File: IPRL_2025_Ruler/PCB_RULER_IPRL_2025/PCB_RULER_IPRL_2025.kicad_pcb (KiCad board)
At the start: 2 copper layers, 155 x 30 mm, 23 parts, among them J102 USB_C_Receptacle_PowerOnly_6P, U101 NE555D, U102 4017

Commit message: Added NFC capabilities
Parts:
- added C102: 220n, Capacitor_SMD:C_0402_1005Metric, F.Cu at (90.5, 106.1)
- added C103: 470p, Capacitor_SMD:C_0402_1005Metric, F.Cu at (85.5, 107.9)
- added D111: LED_Small, LED_SMD:LED_0402_1005Metric, F.Cu at (91.0, 108.3)
- added IC1: NT3H2211W0FTTJ, ruler_footprints_2025:SOP65P490X110-8N, F.Cu at (88.0, 106.2)
- added R104: 47, Resistor_SMD:R_0402_1005Metric, F.Cu at (91.0, 104.0)
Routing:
- net Net-(IC1-LA): track 0.00 -> 10.8 mm, vias 0 -> 2
- net Net-(D111-K): track 0.00 -> 5.90 mm
- net Net-(IC1-VOUT): track 0.00 -> 5.81 mm
- net Net-(D111-A): track 0.00 -> 4.32 mm
- net /9: track 148.1 -> 145.2 mm
- net /1: track 0.00 -> 1.71 mm
- net /5: track 0.00 -> 1.70 mm
- net /TR: track 17.1 -> 18.0 mm
- net /4: track 140.2 -> 139.3 mm

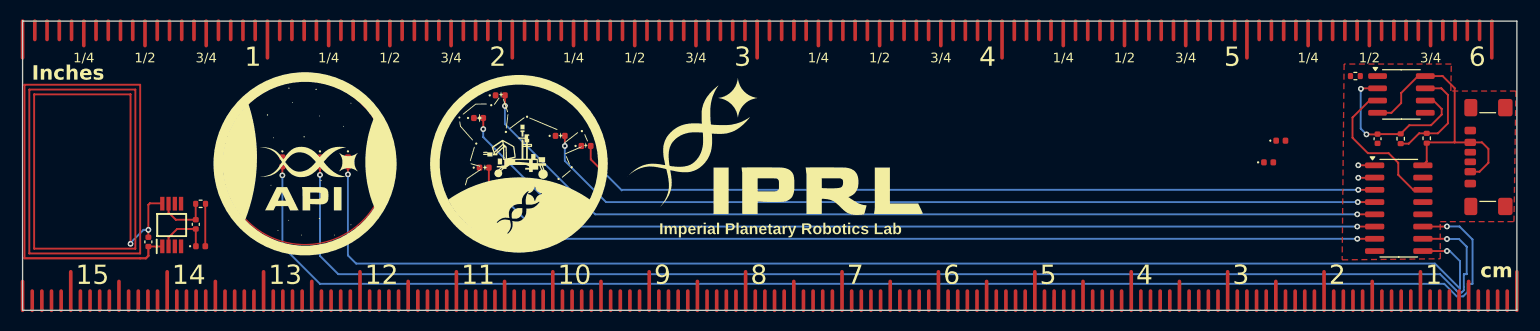
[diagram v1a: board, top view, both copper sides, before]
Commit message: Front side IPRL 2025 Ruler
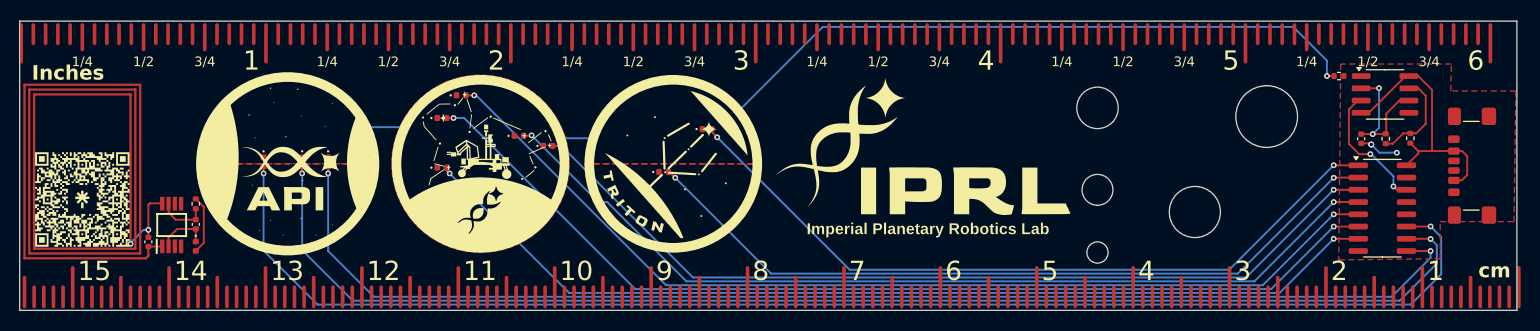
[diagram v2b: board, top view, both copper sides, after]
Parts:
- added G***: LOGO, ruler_footprints_2025:ICRS_LinktreeQR_10mm, F.Cu at (78.7, 103.5)
- added G***: LOGO, ruler_footprints_2025:Trition_Logo, F.Cu at (140.0, 99.8)
- added M2: MountingHole_2.2mm_M2, MountingHole:MountingHole_2.2mm_M2, F.Cu at (184.0, 109.0)
- added REF**: MountingHole_5.3mm_M5, MountingHole:MountingHole_5.3mm_M5, F.Cu at (194.1, 104.8)
- added REF**: MountingHole_4.3mm_M4, MountingHole:MountingHole_4.3mm_M4, F.Cu at (184.0, 94.0)
- added REF**: MountingHole_6.4mm_M6, MountingHole:MountingHole_6.4mm_M6, F.Cu at (201.6, 94.9)
- added REF**: MountingHole_3.2mm_M3, MountingHole:MountingHole_3.2mm_M3, F.Cu at (184.0, 102.5)
- moved D104 64.1 mm to (139.0, 100.6)
- moved D110 58.4 mm to (143.5, 96.2)
- moved G*** 15.3 mm to (166.0, 99.3)
- moved D106 4.39 mm to (116.0, 100.2)
- moved D103 4.26 mm to (124.0, 96.9)
- moved D105 4.05 mm to (118.0, 92.7)
- moved G*** 4.02 mm to (120.0, 99.9)
- moved D109 3.95 mm to (127.0, 98.0)
- moved D107 3.80 mm to (116.0, 95.0)
- moved G*** 3.77 mm to (120.0, 99.7)
- moved D108 2.05 mm to (104.2, 99.6)
- moved D102 1.95 mm to (97.5, 99.6)
- moved J102 1.92 mm to (224.0, 100.0)
- moved G*** 1.90 mm to (100.0, 99.8)
- moved D101 1.85 mm to (101.5, 99.6)
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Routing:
- net /1: track 1.71 -> 80.1 mm, vias 1 -> 2
- net /K: track 0.00 -> 76.7 mm, vias 0 -> 6
- net /5: track 1.70 -> 77.7 mm, vias 1 -> 2
- net /0: track 84.1 -> 93.0 mm
- net /2: track 88.4 -> 96.4 mm
- net /6: track 97.1 -> 103.8 mm
- net /3: track 95.9 -> 102.4 mm
- net /7: track 98.3 -> 104.6 mm
- net /4: track 139.3 -> 135.6 mm
- net /TR: track 18.0 -> 14.4 mm
- net GND: track 0.57 -> 4.10 mm, vias 0 -> 3
- net /8: track 133.1 -> 130.0 mm
- net /9: track 145.2 -> 142.4 mm
- net /CLK: track 15.7 -> 13.8 mm, vias 0 -> 2
- net Net-(D111-A): track 4.32 -> 6.08 mm
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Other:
- board size 155 x 30 mm -> 155.3 x 30 mm

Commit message: Added member names
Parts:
- removed the D104 at (139.0, 100.6)
- removed the D110 at (143.5, 96.2)
- removed the REF** at (201.6, 94.9)
- added D102: LED_Small, LED_SMD:LED_0402_1005Metric, F.Cu at (221.3, 108.8)
- added D106: LED_Small, LED_SMD:LED_0402_1005Metric, F.Cu at (138.9, 100.6)
- added D107: LED_Small, LED_SMD:LED_0402_1005Metric, F.Cu at (143.4, 96.2)
- added G***: LOGO, ruler_footprints_2025:STRAY_WIREFRAME, B.Cu at (169.7, 91.3)
- added G***: LOGO, ruler_footprints_2025:BOBCAT_WIREFRAME, B.Cu at (177.0, 90.3)
- added R103: 430, Resistor_SMD:R_0402_1005Metric, F.Cu at (221.3, 107.7)
- added REF**: PinHeader_1x04_P1.27mm_Vertical, Connector_PinHeader_1.27mm:PinHeader_1x04_P1.27mm_Vertical, F.Cu at (201.6, 109.1)
- added REF**: PinHeader_1x04_P2.00mm_Vertical, Connector_PinHeader_2.00mm:PinHeader_1x04_P2.00mm_Vertical, F.Cu at (205.0, 99.7)
- added REF**: MountingHole_2.7mm_M2.5_DIN965_Pad_TopBottom, MountingHole:MountingHole_2.7mm_M2.5_DIN965_Pad_TopBottom, F.Cu at (185.0, 100.5)
- added REF**: PinHeader_1x04_P2.54mm_Vertical, Connector_PinHeader_2.54mm:PinHeader_1x04_P2.54mm_Vertical, F.Cu at (201.6, 99.4)
- added REF**: PinHeader_1x04_P1.00mm_Vertical, Connector_PinHeader_1.00mm:PinHeader_1x04_P1.00mm_Vertical, F.Cu at (205.0, 108.2)
- M2: value MountingHole_2.2mm_M2 -> MountingHole_2.2mm_M2_DIN965_Pad_TopBottom; footprint MountingHole:MountingHole_2.2mm_M2 -> MountingHole:MountingHole_2.2mm_M2_DIN965_Pad_TopBottom
- REF**: value MountingHole_5.3mm_M5 -> MountingHole_5.3mm_M5_DIN965_Pad_TopBottom; footprint MountingHole:MountingHole_5.3mm_M5 -> MountingHole:MountingHole_5.3mm_M5_DIN965_Pad_TopBottom
- REF**: value MountingHole_3.2mm_M3 -> MountingHole_3.2mm_M3_DIN965_Pad_TopBottom; footprint MountingHole:MountingHole_3.2mm_M3 -> MountingHole:MountingHole_3.2mm_M3_DIN965_Pad_TopBottom
- REF**: value MountingHole_4.3mm_M4 -> MountingHole_4.3mm_M4_DIN965_Pad_TopBottom; footprint MountingHole:MountingHole_4.3mm_M4 -> MountingHole:MountingHole_4.3mm_M4_DIN965_Pad_TopBottom
- moved REF** 15.2 mm to (194.0, 105.5)
- moved R105 10.8 mm to (219.8, 90.7), turned to 90 degrees
- moved REF** 10.3 mm to (194.0, 94.5)
- moved REF** 9.55 mm to (185.0, 93.0)
- moved M2 2.24 mm to (185.0, 107.0)
- renumbered C103 to C101, C101 to C103, D111 to D101, D109 to D103, D101 to D104, D108 to D105, D102 to D108, D103 to D109, D105 to D110, D106 to D111, D107 to D112, IC1 to IC101, J102 to J101, R104 to R101, R103 to R102, R101 to R104, R102 to R105
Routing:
- net /K: track 76.7 -> 87.7 mm
- net +5V: track 27.9 -> 34.8 mm
- net /5: track 77.7 -> 82.4 mm
- net /1: track 80.1 -> 84.4 mm
- net /0: track 93.0 -> 97.1 mm
- net /2: track 96.4 -> 100.1 mm
- net /6: track 103.8 -> 107.2 mm
- net /7: track 104.6 -> 107.9 mm
- net /3: track 102.4 -> 105.4 mm
- net Net-(D102-A): track 0.00 -> 1.16 mm
- net /8: track 130.0 -> 128.9 mm
- net /4: track 135.6 -> 134.6 mm
- net /9: track 142.4 -> 141.5 mm
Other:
- board text added: "1.00"
- board text added: "1.27"
- board text added: "2.00"
- board text added: "2.54"
- board text added: "Adrian Fok"
- board text added: "Aizad Zuber"
- board text added: "Ashley Tan"
- board text added: "BOBCAT 2025"
- board text added: "Ben Smith"
- board text added: "Bjorn Xu"
- board text added: "Daniel Wen"
- board text added: "David Cai"
- board text added: "Eren Seckin"
- board text added: "Filip Szczebak"
- board text added: "Hanka Mehager"
- board text added: "James King"
- board text added: "Jayden Jackson"
- board text added: "Joseph Nestor"
- board text added: "Juan Bustos Lopez"
- board text added: "Jun Yean Yap"
- board text added: "M2.5"
- board text added: "M3"
- board text added: "M4"
- board text added: "M5"
- board text added: "Maciej Grzegorczyk"
- board text added: "Meghna Ranpuria"
- board text added: "Meigan Teo"
- board text added: "Original: Ben Smith Modified by: Ryusei Kinosaki"
- board text added: "Otter Quarks"
- board text added: "Peter Xue"
- board text added: "Pin Headers (mm)"
- board text added: "Poom Chansilpa"
- board text added: "Raphael Sinai"
- board text added: "Sami Marouf"
- board text added: "Samuel Amos-Osebeyo"
- board text added: "SongLi Moey"
- board text added: "Weronika Bogus"
- board text added: "Yeobin Han"
- board text added: "Zhue Jie Tan"

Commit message: IPRL2025Ruler completed
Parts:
- removed the G*** at (140.0, 99.8)
- added G***: LOGO, ruler_footprints_2025:World_Map_2025, B.Cu at (145.1, 98.9)
- added G***: LOGO, ruler_footprints_2025:Triton, B.Cu at (100.2, 91.3)
- added G***: LOGO, ruler_footprints_2025:BOBER_Logo_5mm, B.Cu at (75.2, 100.6)
- added G***: LOGO, ruler_footprints_2025:Triton_Logo, F.Cu at (140.1, 99.9)
- added G***: LOGO, ruler_footprints_2025:API_ROVER_WIREFRAME, B.Cu at (118.6, 90.7)
- added G***: LOGO, ruler_footprints_2025:IPRL_Helix_16mm, B.Cu at (214.6, 99.4)
- moved D107 5.37 mm to (142.3, 101.4)
- moved D106 3.06 mm to (138.7, 97.5)
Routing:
- net /1: track 84.4 -> 87.5 mm
- net /5: track 82.4 -> 81.7 mm
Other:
- board text added: "2022"
- board text added: "2023"
- board text added: "2024"
- board text added: "2025"
- board text added: "2nd team of 20 is formed to build BOBER"
- board text added: "3rd team of 30 is formed to build BOBCat, placing emphasis on robustness"
- board text added: "API 2025"
- board text added: "Anthony Newman"
- board text added: "Ardan Suphi"
- board text added: "BOBCat qualifies for ERC2025 plaing 8th (?)"
- board text added: "Baby Rover is built for prototyping"
- board text added: "Charlotte Cao"
- board text added: "Dominic Peel"
- board text added: "Fatima Sajid"
- board text added: "First team of 11 is formed to build Harbinger"
- board text added: "Hanna Semnanmi"
- board text added: "Harbinger makes 11th from 25 teams, receives presentation award"
- board text added: "IPRL is founded by Filip and Matvey"
- board text added: "IPRL takes part in Great Exhibtion Road Festival"
- board text added: "IPRL visits ESA in Cologne"
- board text added: "IPRL's Voyage"
- board text added: "Ivan Revenga Riesco"
- board text added: "Jenny Shen"
- board text added: "Matvey Boguslavisky"
- board text added: "Project Triton"
- board text added: "Qualification for ERC 2023"
- board text added: "Qualifies for ERC 2024, where BOBER places 17th"
- board text added: "Research Branch is formed"
- board text added: "Research Branch presents their paper to Space Resources Week 2025"
- board text added: "Seamus Kelly"
- board text added: "Sid Halder"
- board text added: "Steven Lee visits IPRL"
- board text added: "Tobiasz Bator"
- board text added: "Yili Chen"

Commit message: Finalised IPRL PCB pre-colour
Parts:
- moved G*** 3.87 mm to (166.0, 90.0)
- moved G*** 2.67 mm to (116.0, 90.0)
- moved G*** 1.64 mm to (176.0, 89.0)
- moved G*** 1.30 mm to (100.2, 90.0)
- moved G*** 1.05 mm to (144.0, 98.9)
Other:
- board text added: "BOBCat qualifies for ERC2025 placing 16th"
- board text removed: "BOBCat qualifies for ERC2025 plaing 8th (?)"
